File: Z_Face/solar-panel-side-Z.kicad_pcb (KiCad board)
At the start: 4 copper layers, 100 x 100 mm, 32 parts, among them J1 CON-5040500591, J2 Face0, J3 Face1, J4 Conn_01x01, J5 Conn_01x01, J6 Conn_01x01, J7 Conn_01x01, J8 Face2, J9 Face3, U1 VEML7700, U2 DRV2605LDGS, U3 MCP9808_DFN

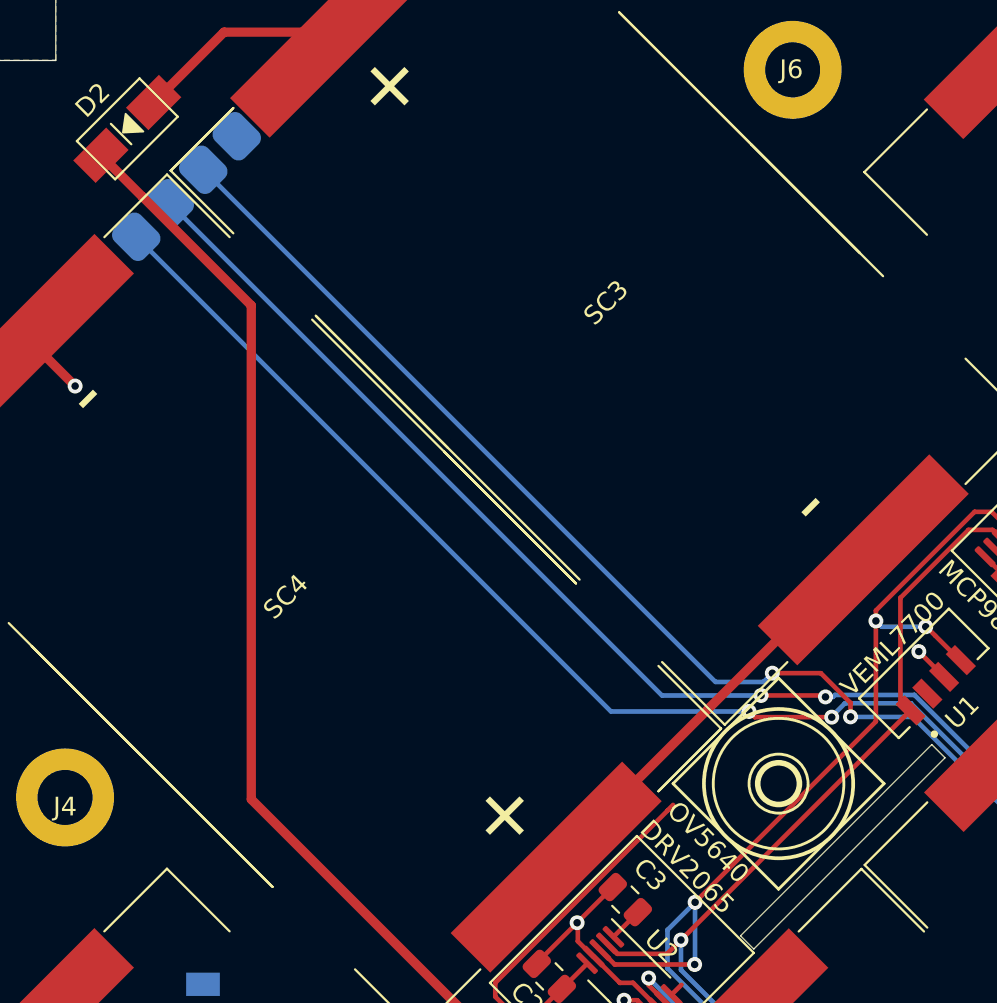
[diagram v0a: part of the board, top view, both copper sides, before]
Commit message: added extra pin to z face
moved it slightly closer also
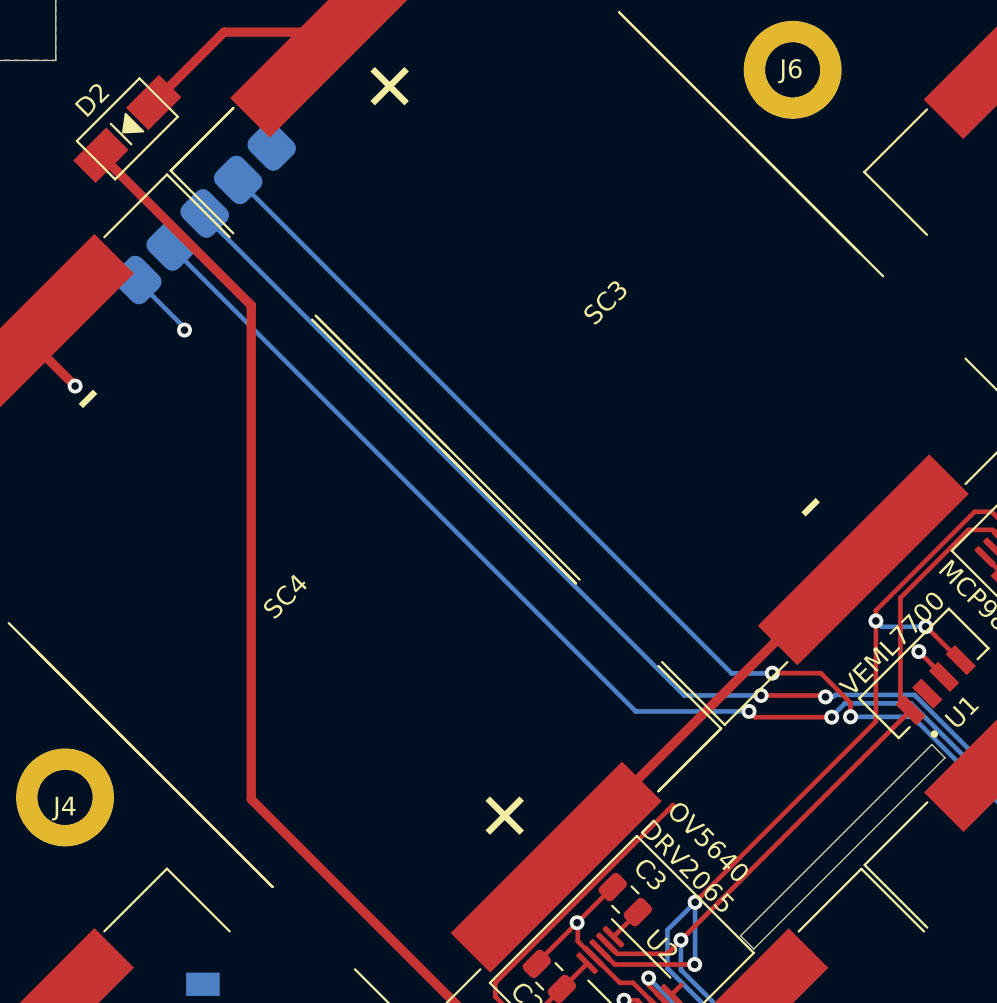
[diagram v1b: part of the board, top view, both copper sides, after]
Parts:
- removed ?: , clipboard:b0880f64-8dff-43fb-af48-c7da55ca08b3
- moved U5 1.71 mm to (114.5, 50.3)
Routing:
- net +3V3: track 39.0 -> 42.7 mm, vias 2 -> 3
- net Camera_Pwr: track 95.0 -> 92.5 mm
- net Camera_SCL: track 100.2 -> 98.2 mm
- net Camera_SDA: track 101.9 -> 99.9 mm
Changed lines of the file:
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@@
     )
   )
-  (footprint "clipboard:b0880f64-8dff-43fb-af48-c7da55ca08b3" (layer "F.Cu")
-    (at 154.4 84.26 45)
-    (fp_text reference "" (at 0 0 45) (layer "F.SilkS")
-        (effects (font (size 1.27 1.27) (thickness 0.15)))
-    )
-    (fp_text value "" (at 0 0 45) (layer "F.SilkS")
-        (effects (font (size 1.27 1.27) (thickness 0.15)))
-    )
-    (fp_line (start -8 -8) (end 0 -8)
-      (stroke (width 0.1524) (type solid)) (layer "F.SilkS"))
-    (fp_line (start -8 0) (end -8 -8)
-      (stroke (width 0.1524) (type solid)) (layer "F.SilkS"))
-    (fp_line (start 0 -8) (end 0 0)
-      (stroke (width 0.1524) (type solid)) (layer "F.SilkS"))
-    (fp_line (start 0 0) (end -8 0)
-      (stroke (width 0.1524) (type solid)) (layer "F.SilkS"))
-    (fp_circle (center -4 -4) (end -2.881969 -4)
-      (stroke (width 0.3) (type solid)) (fill none) (layer "F.SilkS"))
-    (fp_circle (center -4 -4) (end -2.418863 -4)
-      (stroke (width 0.1524) (type solid)) (fill none) (layer "F.SilkS"))
-    (fp_circle (center -4 -4) (end -0.5 -4)
-      (stroke (width 0.1524) (type solid)) (fill none) (layer "F.SilkS"))
-    (fp_circle (center -4 -4) (end 0 -4)
-      (stroke (width 0.2) (type solid)) (fill none) (layer "F.SilkS"))
-  )
   (footprint "Resistor_SMD:R_0603_1608Metric" (layer "F.Cu")
     (at 165.419368 66.315938 -45)
@@
   )
   (footprint "camera_daughter:camera_daughter" (layer "B.Cu")
-    (at 113.261397 49.12859 -135)
+    (at 114.546397 50.26359 -135)
     (property "Sheetfile" "solar-panel-side-Z.kicad_sch")
     (property "Sheetname" "")
@@
     (fp_rect (start -11.03 -3.67) (end 10.44 -41.5)
       (stroke (width 0.12) (type default)) (fill none) (layer "B.SilkS"))
-    (pad "1" smd roundrect (at -4.25 -4.86 135) (size 2.27 2) (layers "B.Cu" "B.Paste" "B.Mask") (roundrect_rratio 0.25)
+    (pad "1" smd roundrect (at -5.08 -4.86 135) (size 2.27 2) (layers "B.Cu" "B.Paste" "B.Mask") (roundrect_rratio 0.25)
       (net 1 "GND") (pinfunction "GND") (pintype "input") (thermal_bridge_angle 45))
-    (pad "2" smd roundrect (at -1.71 -4.86 135) (size 2.27 2) (layers "B.Cu" "B.Paste" "B.Mask") (roundrect_rratio 0.25)
-      (net 38 "Camera_Pwr") (pinfunction "3V3") (pintype "input") (thermal_bridge_angle 45))
-    (pad "3" smd roundrect (at 0.83 -4.86 135) (size 2.27 2) (layers "B.Cu" "B.Paste" "B.Mask") (roundrect_rratio 0.25)
+    (pad "2" smd roundrect (at -2.54 -4.86 135) (size 2.27 2) (layers "B.Cu" "B.Paste" "B.Mask") (roundrect_rratio 0.25)
+      (net 38 "Camera_Pwr") (pinfunction "ctrl") (pintype "input") (thermal_bridge_angle 45))
+    (pad "3" smd roundrect (at 0 -4.86 135) (size 2.27 2) (layers "B.Cu" "B.Paste" "B.Mask") (roundrect_rratio 0.25)
       (net 40 "Camera_SDA") (pinfunction "SDA") (pintype "input") (thermal_bridge_angle 45))
-    (pad "4" smd roundrect (at 3.37 -4.86 135) (size 2.27 2) (layers "B.Cu" "B.Paste" "B.Mask") (roundrect_rratio 0.25)
+    (pad "4" smd roundrect (at 2.54 -4.826 135) (size 2.27 2) (layers "B.Cu" "B.Paste" "B.Mask") (roundrect_rratio 0.25)
       (net 39 "Camera_SCL") (pinfunction "SCL") (pintype "input") (thermal_bridge_angle 45))
+    (pad "5" smd roundrect (at 5.08 -4.826 135) (size 2.27 2) (layers "B.Cu" "B.Paste" "B.Mask") (roundrect_rratio 0.25)
+      (net 2 "+3V3") (pinfunction "3V3") (pintype "input") (thermal_bridge_angle 45))
   )
   (gr_poly
@@
   (segment (start 142.806126 85.683874) (end 143.09 85.4) (width 0.25) (layer "F.Cu") (net 2))
   (segment (start 137.128765 95.263232) (end 137.096768 95.263232) (width 0.25) (layer "F.Cu") (net 2))
+  (via (at 116.9 59.95) (size 0.8) (drill 0.4) (layers "F.Cu" "B.Cu") (net 2))
   (via (at 165.14 72.79) (size 0.8) (drill 0.4) (layers "F.Cu" "B.Cu") (net 2))
   (via (at 165.98 102) (size 0.8) (drill 0.4) (layers "F.Cu" "B.Cu") (net 2))
+  (segment (start 114.366792 57.291792) (end 114.366792 57.26819) (width 0.25) (layer "B.Cu") (net 2))
   (segment (start 163.426726 110.24) (end 165.98 107.686726) (width 0.25) (layer "B.Cu") (net 2))
+  (segment (start 116.9 59.825) (end 114.366792 57.291792) (width 0.25) (layer "B.Cu") (net 2))
   (segment (start 162.44 110.24) (end 163.426726 110.24) (width 0.25) (layer "B.Cu") (net 2))
+  (segment (start 116.9 59.95) (end 116.9 59.825) (width 0.25) (layer "B.Cu") (net 2))
   (segment (start 165.98 107.686726) (end 165.98 102) (width 0.25) (layer "B.Cu") (net 2))
   (segment (start 113.41 124.31) (end 113.41 123.99) (width 0.5) (layer "F.Cu") (net 3))
@@
   (via (at 152.6 80.68) (size 0.8) (drill 0.4) (layers "F.Cu" "B.Cu") (net 38))
   (segment (start 166.75 100.54) (end 162.62 96.41) (width 0.25) (layer "B.Cu") (net 38))
-  (segment (start 145.361113 78.81) (end 117.907089 51.355976) (width 0.25) (layer "B.Cu") (net 38))
   (segment (start 155.92962 80.68) (end 152.6 80.68) (width 0.25) (layer "B.Cu") (net 38))
   (segment (start 163.426726 117.86) (end 166.75 114.536726) (width 0.25) (layer "B.Cu") (net 38))
+  (segment (start 148.40996 78.33996) (end 148.39992 78.35) (width 0.25) (layer "B.Cu") (net 38))
+  (segment (start 119.779078 51.904078) (end 119.778987 51.904078) (width 0.25) (layer "B.Cu") (net 38))
   (segment (start 162.62 96.41) (end 162.62 87.37038) (width 0.25) (layer "B.Cu") (net 38))
   (segment (start 166.75 114.536726) (end 166.75 100.54) (width 0.25) (layer "B.Cu") (net 38))
   (segment (start 162.62 87.37038) (end 155.92962 80.68) (width 0.25) (layer "B.Cu") (net 38))
-  (segment (start 148.40996 78.33996) (end 147.93992 78.81) (width 0.25) (layer "B.Cu") (net 38))
   (segment (start 162.44 117.86) (end 163.426726 117.86) (width 0.25) (layer "B.Cu") (net 38))
-  (segment (start 147.93992 78.81) (end 145.361113 78.81) (width 0.25) (layer "B.Cu") (net 38))
+  (segment (start 148.39992 78.35) (end 146.225 78.35) (width 0.25) (layer "B.Cu") (net 38))
+  (segment (start 146.225 78.35) (end 119.779078 51.904078) (width 0.25) (layer "B.Cu") (net 38))
   (segment (start 147.467299 80.697299) (end 151.592701 80.697299) (width 0.25) (layer "F.Cu") (net 39))
   (segment (start 147.16 80.39) (end 147.467299 80.697299) (width 0.25) (layer "F.Cu") (net 39))
@@
   (via (at 151.592701 80.697299) (size 0.8) (drill 0.4) (layers "F.Cu" "B.Cu") (net 39))
   (segment (start 167.2 100.353604) (end 167.2 116.626726) (width 0.25) (layer "B.Cu") (net 39))
-  (segment (start 147.16 80.39) (end 139.756907 80.39) (width 0.25) (layer "B.Cu") (net 39))
   (segment (start 151.592701 80.661994) (end 152.299695 79.955) (width 0.25) (layer "B.Cu") (net 39))
+  (segment (start 147.16 80.39) (end 141.09 80.39) (width 0.25) (layer "B.Cu") (net 39))
   (segment (start 151.592701 80.697299) (end 151.592701 80.661994) (width 0.25) (layer "B.Cu") (net 39))
   (segment (start 163.08 96.233604) (end 167.2 100.353604) (width 0.25) (layer "B.Cu") (net 39))
-  (segment (start 139.756907 80.39) (end 114.314986 54.948079) (width 0.25) (layer "B.Cu") (net 39))
+  (segment (start 141.09 80.39) (end 116.172139 55.472139) (width 0.25) (layer "B.Cu") (net 39))
   (segment (start 167.2 116.626726) (end 163.426726 120.4) (width 0.25) (layer "B.Cu") (net 39))
   (segment (start 152.299695 79.955) (end 155.841016 79.955) (width 0.25) (layer "B.Cu") (net 39))
   (segment (start 155.841016 79.955) (end 163.08 87.193984) (width 0.25) (layer "B.Cu") (net 39))
   (segment (start 163.426726 120.4) (end 162.44 120.4) (width 0.25) (layer "B.Cu") (net 39))
+  (segment (start 116.172139 55.472139) (end 116.162843 55.472139) (width 0.25) (layer "B.Cu") (net 39))
   (segment (start 163.08 87.193984) (end 163.08 96.233604) (width 0.25) (layer "B.Cu") (net 39))
   (segment (start 151.179902 79.5345) (end 147.806483 79.5345) (width 0.25) (layer "F.Cu") (net 40))
@@
   (via (at 151.257701 79.612299) (size 0.8) (drill 0.4) (layers "F.Cu" "B.Cu") (net 40))
   (via (at 147.806483 79.5345) (size 0.8) (drill 0.4) (layers "F.Cu" "B.Cu") (net 40))
-  (segment (start 142.493509 79.5345) (end 116.111037 53.152028) (width 0.25) (layer "B.Cu") (net 40))
+  (segment (start 143.6845 79.5345) (end 117.982936 53.832936) (width 0.25) (layer "B.Cu") (net 40))
   (segment (start 163.68 96.19) (end 167.65 100.16) (width 0.25) (layer "B.Cu") (net 40))
   (segment (start 163.426726 122.94) (end 162.44 122.94) (width 0.25) (layer "B.Cu") (net 40))
@@
   (segment (start 151.257701 79.612299) (end 151.652396 79.612299) (width 0.25) (layer "B.Cu") (net 40))
   (segment (start 167.65 100.16) (end 167.65 118.716726) (width 0.25) (layer "B.Cu") (net 40))
-  (segment (start 147.806483 79.5345) (end 142.493509 79.5345) (width 0.25) (layer "B.Cu") (net 40))
   (segment (start 163.68 87.157588) (end 163.68 96.19) (width 0.25) (layer "B.Cu") (net 40))
   (segment (start 167.65 118.716726) (end 163.426726 122.94) (width 0.25) (layer "B.Cu") (net 40))
+  (segment (start 117.982936 53.832936) (end 117.982936 53.700129) (width 0.25) (layer "B.Cu") (net 40))
+  (segment (start 147.806483 79.5345) (end 143.6845 79.5345) (width 0.25) (layer "B.Cu") (net 40))
   (zone (net 2) (net_name "+3V3") (layer "F.Cu") (hatch edge 0.508)
     (connect_pads (clearance 0.508))

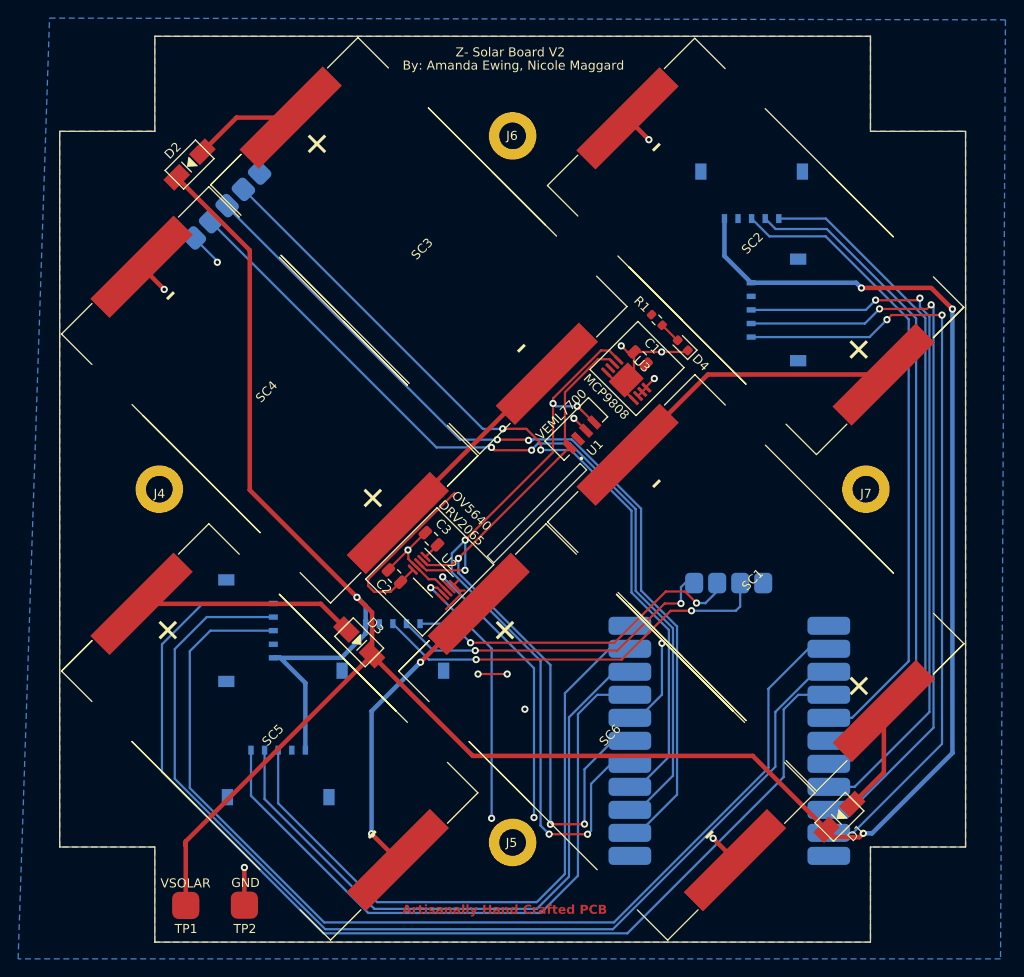
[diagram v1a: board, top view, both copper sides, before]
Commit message: Fixed Antenna Board
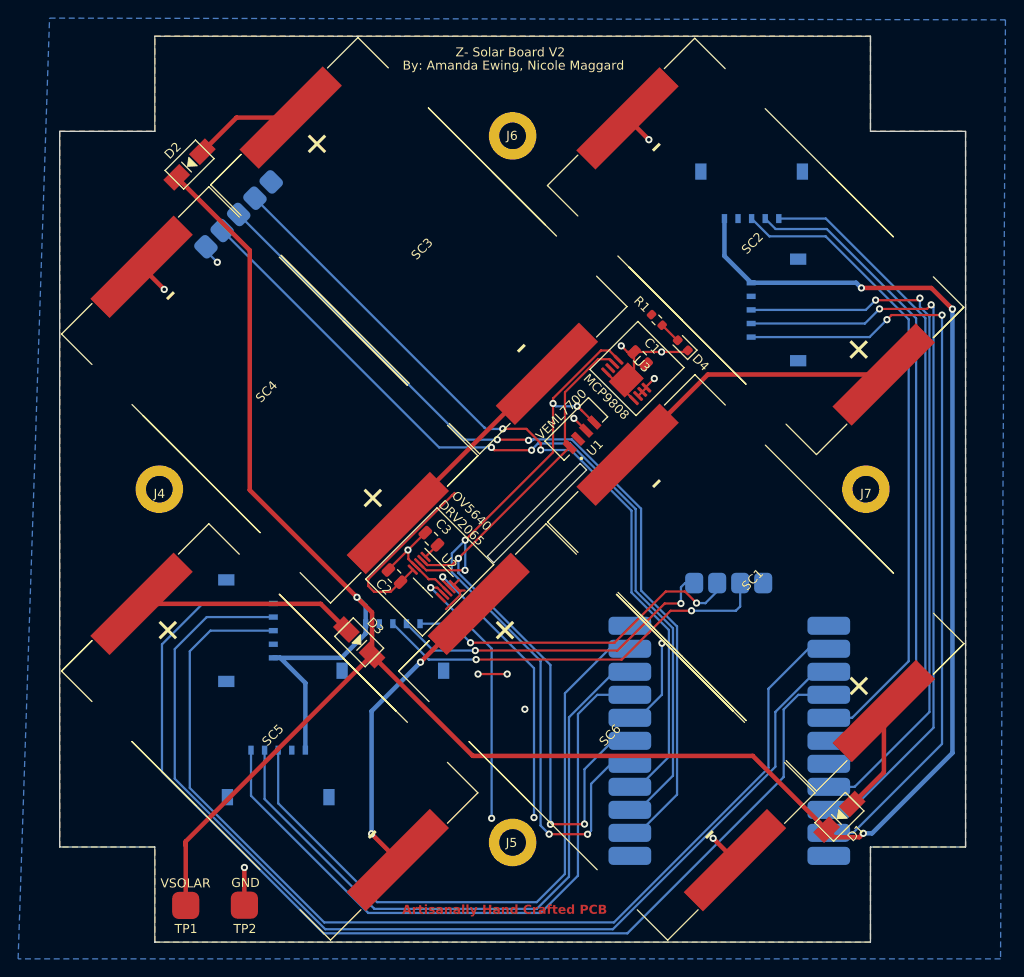
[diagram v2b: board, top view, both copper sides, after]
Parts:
- moved U5 1.61 mm to (115.8, 51.2)
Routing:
- net Camera_SDA: track 99.9 -> 98.1 mm
- net Camera_SCL: track 98.2 -> 96.5 mm
- net Camera_Pwr: track 92.5 -> 90.9 mm
- net +3V3: track 42.7 -> 41.4 mm
